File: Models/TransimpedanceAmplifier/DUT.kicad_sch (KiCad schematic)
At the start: 1 part

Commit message: Save progress
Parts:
- removed JP2: Jumper_2_Open, symbol Jumper:Jumper_2_Open
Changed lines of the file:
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@@
-		)
-	)
-	(wire
-		(pts
-			(xy 144.78 91.44) (xy 149.86 91.44)
-		)
-		(stroke
-			(width 0)
-			(type default)
-		)
-	)
-	(wire
-		(pts
-			(xy 160.02 91.44) (xy 165.1 91.44)
-		)
-		(stroke
-			(width 0)
-			(type default)
-		)
-	)
-	(hierarchical_label "Output"
-		(shape output)
-		(at 165.1 91.44 0)
-		(effects
-			(font
-				(size 1.27 1.27)
-			)
-			(justify left)
-		)
-	)
-	(hierarchical_label "Input"
-		(shape input)
-		(at 144.78 91.44 180)
-		(effects
-			(font
-				(size 1.27 1.27)
-			)
-			(justify right)
-		)
-	)
-	(symbol
-		(lib_id "Jumper:Jumper_2_Open")
-		(at 154.94 91.44 0)
-		(unit 1)
-		(exclude_from_sim no)
-		(in_bom yes)
-		(on_board yes)
-		(dnp no)
-		(fields_autoplaced yes)
-		(property "Reference" "JP2"
-			(at 154.94 85.09 0)
-			(effects
-				(font
-					(size 1.27 1.27)
-				)
-			)
-		)
-		(property "Value" "Jumper_2_Open"
-			(at 154.94 87.63 0)
-			(effects
-				(font
-					(size 1.27 1.27)
-				)
-			)
-		)
-		(property "Footprint" ""
-			(at 154.94 91.44 0)
-			(effects
-				(font
-					(size 1.27 1.27)
-				)
-				(hide yes)
-			)
-		)
-		(property "Datasheet" "~"
-			(at 154.94 91.44 0)
-			(effects
-				(font
-					(size 1.27 1.27)
-				)
-				(hide yes)
-			)
-		)
-		(property "Description" "Jumper, 2-pole, open"
-			(at 154.94 91.44 0)
-			(effects
-				(font
-					(size 1.27 1.27)
-				)
-				(hide yes)
-			)
-		)
-		(pin "1"
-		)
-		(pin "2"
-		)
-		(instances
-			(project ""
-				(path "/ec9f2ae3-e40d-40eb-9760-2b611ee8efd1/dc71cb80-a5fe-4d35-8e0a-2347d37b6518"
-					(reference "JP2")
-					(unit 1)
-				)
-			)
 		)
 	)

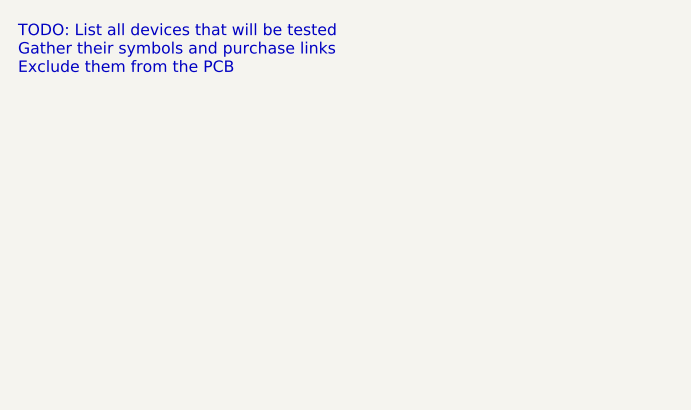
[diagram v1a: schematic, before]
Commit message: Assigned all the SPI pins
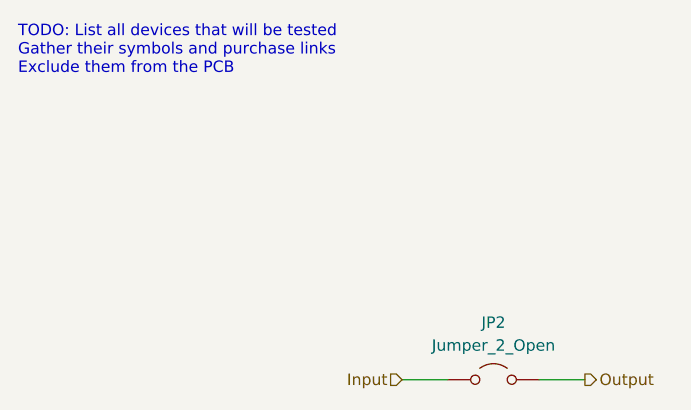
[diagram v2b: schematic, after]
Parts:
- added JP2: Jumper_2_Open, symbol Jumper:Jumper_2_Open
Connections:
- new net Input: JP2.1 (A)
- new net Output: JP2.2 (B)
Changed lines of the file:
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@@
+		)
+	)
+	(wire
+		(pts
+			(xy 144.78 91.44) (xy 149.86 91.44)
+		)
+		(stroke
+			(width 0)
+			(type default)
+		)
+	)
+	(wire
+		(pts
+			(xy 160.02 91.44) (xy 165.1 91.44)
+		)
+		(stroke
+			(width 0)
+			(type default)
+		)
+	)
+	(hierarchical_label "Output"
+		(shape output)
+		(at 165.1 91.44 0)
+		(effects
+			(font
+				(size 1.27 1.27)
+			)
+			(justify left)
+		)
+	)
+	(hierarchical_label "Input"
+		(shape input)
+		(at 144.78 91.44 180)
+		(effects
+			(font
+				(size 1.27 1.27)
+			)
+			(justify right)
+		)
+	)
+	(symbol
+		(lib_id "Jumper:Jumper_2_Open")
+		(at 154.94 91.44 0)
+		(unit 1)
+		(exclude_from_sim no)
+		(in_bom yes)
+		(on_board yes)
+		(dnp no)
+		(fields_autoplaced yes)
+		(property "Reference" "JP2"
+			(at 154.94 85.09 0)
+			(effects
+				(font
+					(size 1.27 1.27)
+				)
+			)
+		)
+		(property "Value" "Jumper_2_Open"
+			(at 154.94 87.63 0)
+			(effects
+				(font
+					(size 1.27 1.27)
+				)
+			)
+		)
+		(property "Footprint" ""
+			(at 154.94 91.44 0)
+			(effects
+				(font
+					(size 1.27 1.27)
+				)
+				(hide yes)
+			)
+		)
+		(property "Datasheet" "~"
+			(at 154.94 91.44 0)
+			(effects
+				(font
+					(size 1.27 1.27)
+				)
+				(hide yes)
+			)
+		)
+		(property "Description" "Jumper, 2-pole, open"
+			(at 154.94 91.44 0)
+			(effects
+				(font
+					(size 1.27 1.27)
+				)
+				(hide yes)
+			)
+		)
+		(pin "1"
+		)
+		(pin "2"
+		)
+		(instances
+			(project ""
+				(path "/ec9f2ae3-e40d-40eb-9760-2b611ee8efd1/dc71cb80-a5fe-4d35-8e0a-2347d37b6518"
+					(reference "JP2")
+					(unit 1)
+				)
+			)
 		)
 	)
